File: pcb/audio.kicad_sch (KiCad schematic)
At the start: 30 parts, among them J3 AudioJack4, U3 ES7210, U5 ES8311, U6 IS31AP2005

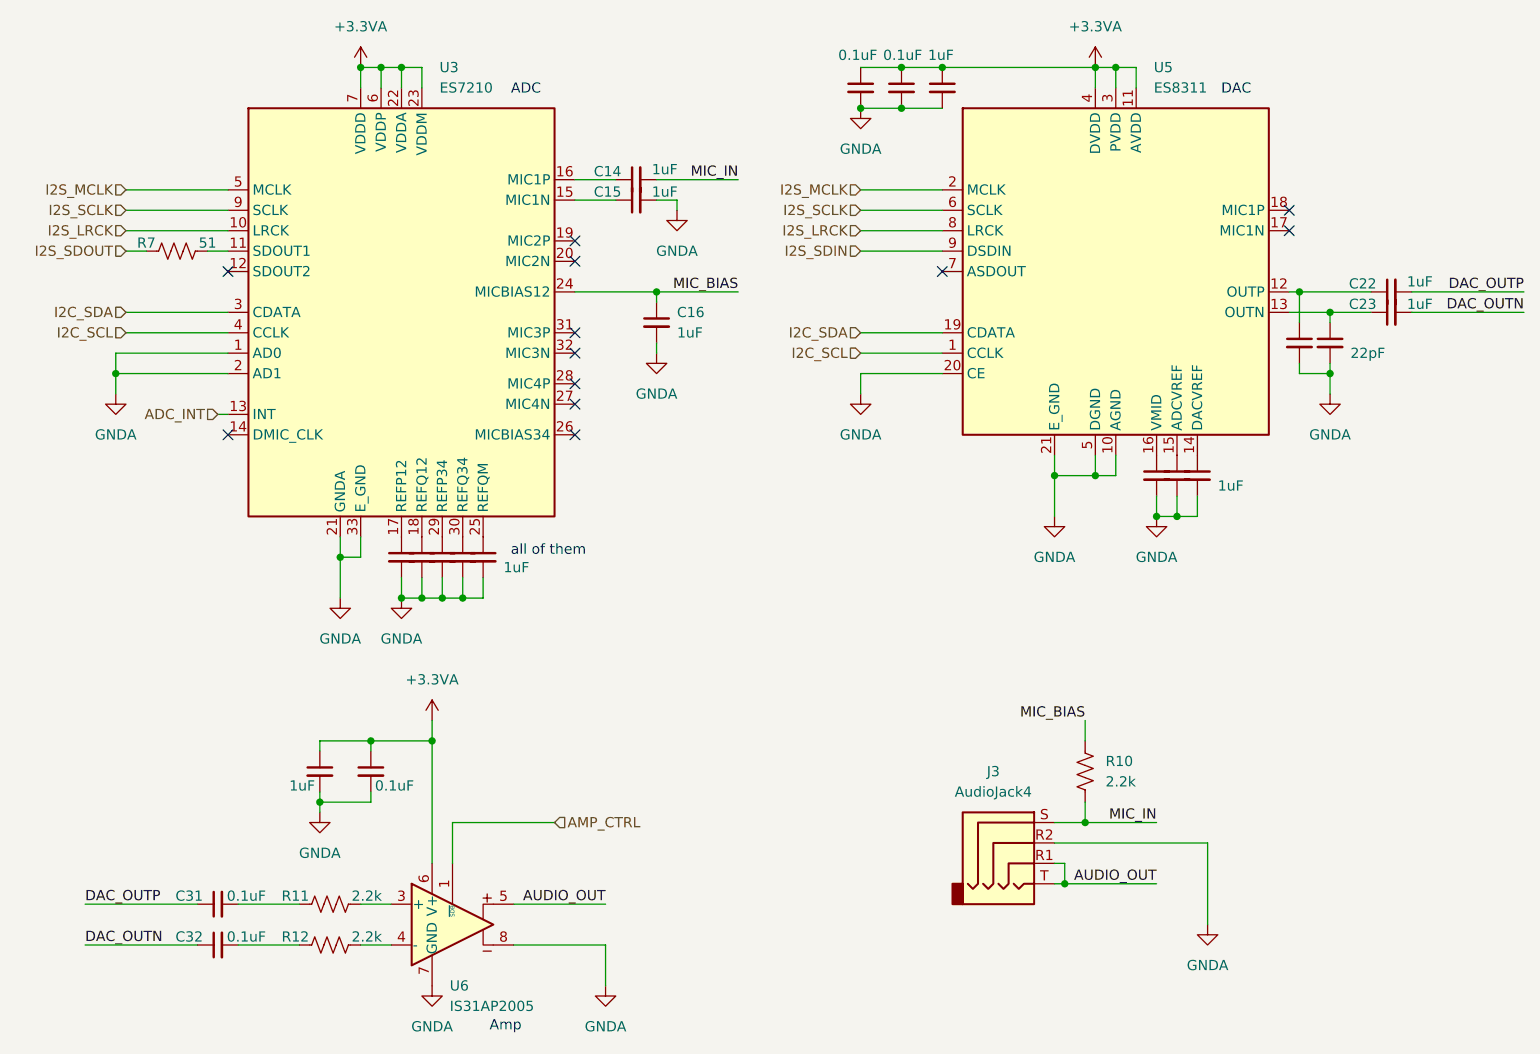
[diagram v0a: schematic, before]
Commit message: pcb: Renumber parts
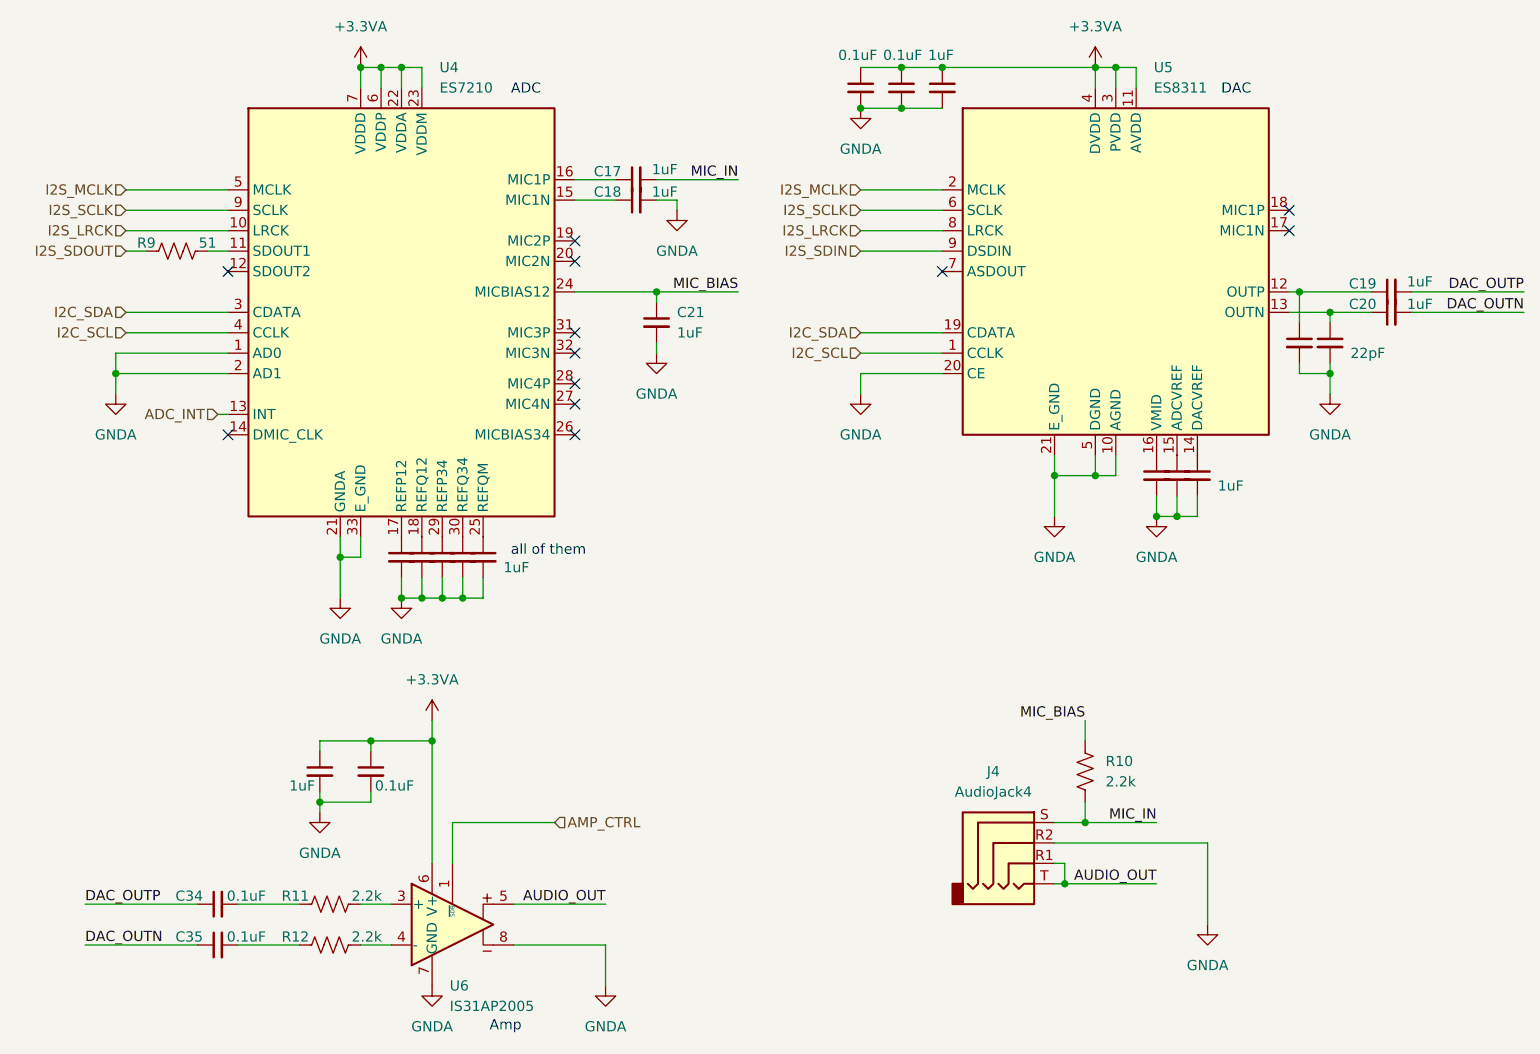
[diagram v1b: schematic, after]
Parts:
- renumbered C26 to C14, C25 to C15, C24 to C16, C14 to C17, C15 to C18, C22 to C19, C23 to C20, C16 to C21, C27 to C22, C28 to C23, C19 to C24, C20 to C25, C21 to C26, C9 to C27, C10 to C28, C11 to C29, C12 to C30, C13 to C31, C30 to C32, C29 to C33, C31 to C34, C32 to C35, J3 to J4, R7 to R9, U3 to U4

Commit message: pcb: Assigned footprints (the more trivial ones)
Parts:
- C14, C15, C16, C17, C18, C19, C20, C21, C22, C23, C24, C25, C26, C27, C28, C29, C30, C31, C32, C33, C34, C35: footprint (none) -> Capacitor_SMD:C_0603_1608Metric
- R10, R11, R12, R9: footprint (none) -> Resistor_SMD:R_0603_1608Metric
- U4: footprint (none) -> Package_DFN_QFN:QFN-32-1EP_4x4mm_P0.4mm_EP2.9x2.9mm
- U5: footprint (none) -> Package_DFN_QFN:QFN-20-1EP_3x3mm_P0.4mm_EP1.65x1.65mm
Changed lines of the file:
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@@
 			)
 		)
-		(property "Footprint" ""
+		(property "Footprint" "Capacitor_SMD:C_0603_1608Metric"
 			(at 82.55 93.98 0)
 			(effects
@@
 			)
 		)
-		(property "Footprint" ""
+		(property "Footprint" "Resistor_SMD:R_0603_1608Metric"
 			(at 73.914 141.224 90)
 			(effects
@@
 			)
 		)
-		(property "Footprint" ""
+		(property "Footprint" "Capacitor_SMD:C_0603_1608Metric"
 			(at 59.69 142.24 0)
 			(effects
@@
 			)
 		)
-		(property "Footprint" ""
+		(property "Footprint" "Capacitor_SMD:C_0603_1608Metric"
 			(at 181.61 83.82 0)
 			(effects
@@
 			)
 		)
-		(property "Footprint" ""
+		(property "Footprint" "Capacitor_SMD:C_0603_1608Metric"
 			(at 90.17 93.98 0)
 			(effects
@@
 			)
 		)
-		(property "Footprint" ""
+		(property "Footprint" "Capacitor_SMD:C_0603_1608Metric"
 			(at 149.86 35.56 0)
 			(effects
@@
 			)
 		)
-		(property "Footprint" ""
+		(property "Footprint" "Capacitor_SMD:C_0603_1608Metric"
 			(at 85.09 93.98 0)
 			(effects
@@
 			)
 		)
-		(property "Footprint" ""
+		(property "Footprint" "Capacitor_SMD:C_0603_1608Metric"
 			(at 111.76 46.99 0)
 			(effects
@@
 			)
 		)
-		(property "Footprint" ""
+		(property "Footprint" "Capacitor_SMD:C_0603_1608Metric"
 			(at 139.7 35.56 0)
 			(effects
@@
 			)
 		)
-		(property "Footprint" ""
+		(property "Footprint" "Resistor_SMD:R_0603_1608Metric"
 			(at 73.914 136.144 90)
 			(effects
@@
 			)
 		)
-		(property "Footprint" ""
+		(property "Footprint" "Capacitor_SMD:C_0603_1608Metric"
 			(at 144.78 35.56 0)
 			(effects
@@
 			)
 		)
-		(property "Footprint" ""
+		(property "Footprint" "Package_DFN_QFN:QFN-32-1EP_4x4mm_P0.4mm_EP2.9x2.9mm"
 			(at 82.55 96.52 0)
 			(effects
@@
 			)
 		)
-		(property "Footprint" ""
+		(property "Footprint" "Capacitor_SMD:C_0603_1608Metric"
 			(at 72.39 120.65 0)
 			(effects
@@
 			)
 		)
-		(property "Footprint" ""
+		(property "Footprint" "Capacitor_SMD:C_0603_1608Metric"
 			(at 198.12 67.31 0)
 			(effects
@@
 			)
 		)
-		(property "Footprint" ""
+		(property "Footprint" "Capacitor_SMD:C_0603_1608Metric"
 			(at 179.07 83.82 0)
 			(effects
@@
 			)
 		)
-		(property "Footprint" ""
+		(property "Footprint" "Capacitor_SMD:C_0603_1608Metric"
 			(at 205.74 63.5 0)
 			(effects
@@
 			)
 		)
-		(property "Footprint" ""
+		(property "Footprint" "Resistor_SMD:R_0603_1608Metric"
 			(at 168.656 120.904 90)
 			(effects
@@
 			)
 		)
-		(property "Footprint" ""
+		(property "Footprint" "Capacitor_SMD:C_0603_1608Metric"
 			(at 87.63 93.98 0)
 			(effects
@@
 			)
 		)
-		(property "Footprint" ""
+		(property "Footprint" "Capacitor_SMD:C_0603_1608Metric"
 			(at 205.74 60.96 0)
 			(effects
@@
 			)
 		)
-		(property "Footprint" ""
+		(property "Footprint" "Capacitor_SMD:C_0603_1608Metric"
 			(at 92.71 93.98 0)
 			(effects
@@
 			)
 		)
-		(property "Footprint" ""
+		(property "Footprint" "Capacitor_SMD:C_0603_1608Metric"
 			(at 59.69 137.16 0)
 			(effects
@@
 			)
 		)
-		(property "Footprint" ""
+		(property "Footprint" "Capacitor_SMD:C_0603_1608Metric"
 			(at 78.74 120.65 0)
 			(effects
@@
 			)
 		)
-		(property "Footprint" ""
+		(property "Footprint" "Capacitor_SMD:C_0603_1608Metric"
 			(at 111.76 49.53 0)
 			(effects
@@
 			)
 		)
-		(property "Footprint" ""
+		(property "Footprint" "Capacitor_SMD:C_0603_1608Metric"
 			(at 194.31 67.31 0)
 			(effects
@@
 			)
 		)
-		(property "Footprint" ""
+		(property "Footprint" "Capacitor_SMD:C_0603_1608Metric"
 			(at 114.3 64.77 0)
 			(effects
@@
 			)
 		)
-		(property "Footprint" ""
+		(property "Footprint" "Resistor_SMD:R_0603_1608Metric"
 			(at 54.864 54.864 90)
 			(effects
@@
 			)
 		)
-		(property "Footprint" ""
+		(property "Footprint" "Capacitor_SMD:C_0603_1608Metric"
 			(at 176.53 83.82 0)
 			(effects
@@
 			)
 		)
-		(property "Footprint" ""
+		(property "Footprint" "Package_DFN_QFN:QFN-20-1EP_3x3mm_P0.4mm_EP1.65x1.65mm"
 			(at 171.45 86.36 0)
 			(effects
